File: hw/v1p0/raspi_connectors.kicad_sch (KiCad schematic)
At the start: 3 parts, among them J8 Raspberry_Pi_2_3

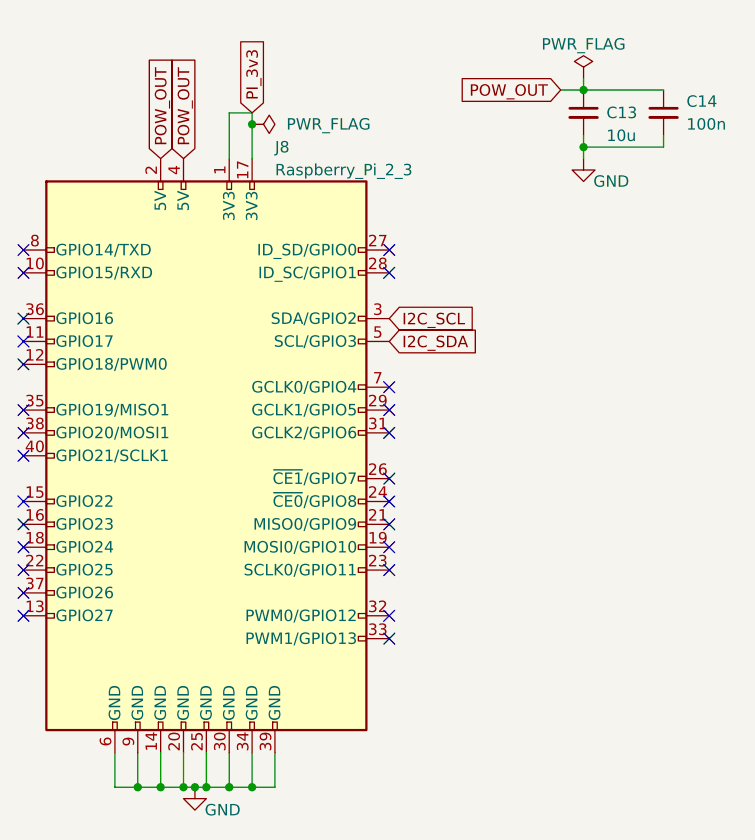
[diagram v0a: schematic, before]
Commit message: Last version before removing mosfet
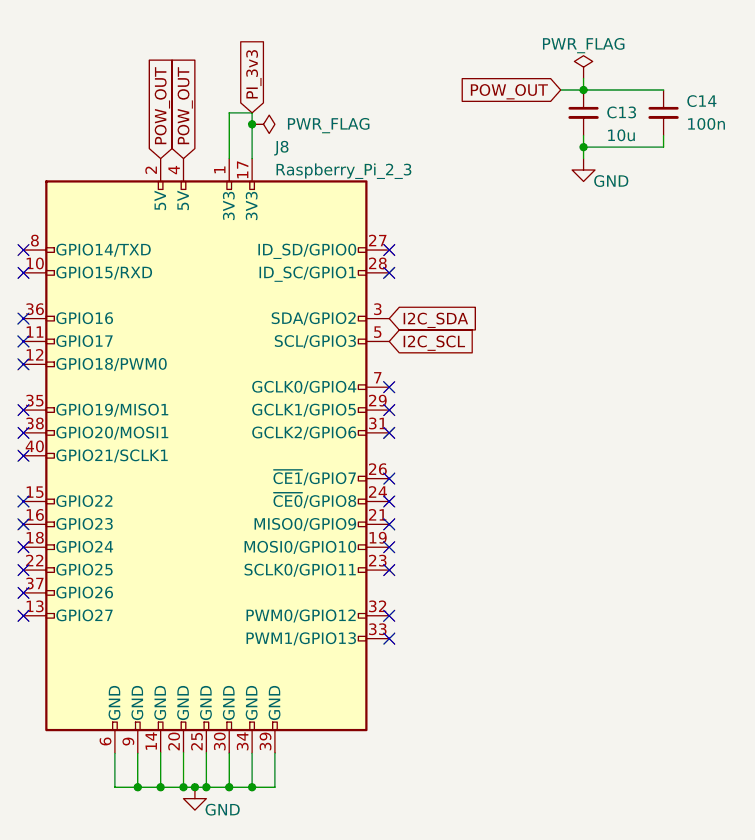
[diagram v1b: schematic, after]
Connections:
- net I2C_SCL: now also J8.5 (SCL/GPIO3); no longer J8.3 (SDA/GPIO2)
- net I2C_SDA: now also J8.3 (SDA/GPIO2); no longer J8.5 (SCL/GPIO3)
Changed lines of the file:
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@@
     )
   )
-  (global_label "I2C_SCL" (shape input) (at 81.28 49.53 0) (fields_autoplaced)
+  (global_label "I2C_SCL" (shape input) (at 81.28 52.07 0) (fields_autoplaced)
     (effects (font (size 1.27 1.27)) (justify left))
-    (property "Intersheet References" "${INTERSHEET_REFS}" (id 0) (at 91.2526 49.4506 0)
+    (property "Intersheet References" "${INTERSHEET_REFS}" (id 0) (at 91.2526 51.9906 0)
       (effects (font (size 1.27 1.27)) (justify left) hide)
     )
@@
     )
   )
-  (global_label "I2C_SDA" (shape input) (at 81.28 52.07 0) (fields_autoplaced)
+  (global_label "I2C_SDA" (shape input) (at 81.28 49.53 0) (fields_autoplaced)
     (effects (font (size 1.27 1.27)) (justify left))
-    (property "Intersheet References" "${INTERSHEET_REFS}" (id 0) (at 91.3131 51.9906 0)
+    (property "Intersheet References" "${INTERSHEET_REFS}" (id 0) (at 91.3131 49.4506 0)
       (effects (font (size 1.27 1.27)) (justify left) hide)
     )

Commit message: Removed Mosfet - release candidate 1.0
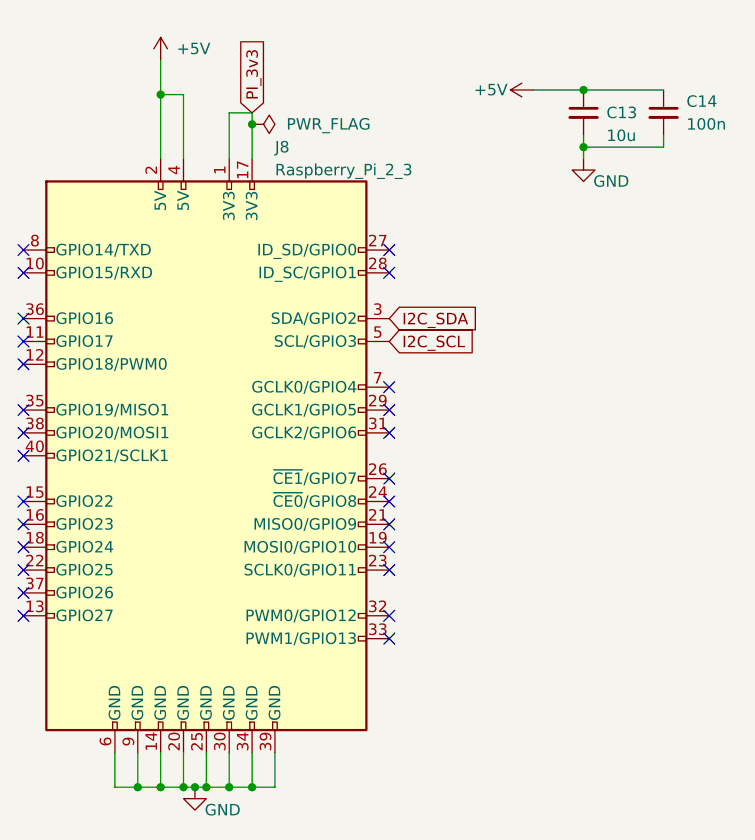
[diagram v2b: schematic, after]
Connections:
- net POW_OUT renamed +5V
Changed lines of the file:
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@@
   (junction (at 60.96 101.6) (diameter 0) (color 0 0 0 0)
+  )
+  (junction (at 55.88 24.638) (diameter 0) (color 0 0 0 0)
   )
   (no_connect (at 81.28 59.69))
@@
     (stroke (width 0) (type default) (color 0 0 0 0))
   )
+  (wire (pts (xy 55.88 24.638) (xy 55.88 31.75))
+    (stroke (width 0) (type default) (color 0 0 0 0))
+  )
   (wire (pts (xy 102.87 24.13) (xy 111.76 24.13))
     (stroke (width 0) (type default) (color 0 0 0 0))
@@
     (stroke (width 0) (type default) (color 0 0 0 0))
   )
-  (wire (pts (xy 102.87 22.86) (xy 102.87 24.13))
-    (stroke (width 0) (type default) (color 0 0 0 0))
-  )
   (wire (pts (xy 68.58 97.79) (xy 68.58 101.6))
     (stroke (width 0) (type default) (color 0 0 0 0))
@@
     (stroke (width 0) (type default) (color 0 0 0 0))
   )
-  (wire (pts (xy 100.33 24.13) (xy 102.87 24.13))
+  (wire (pts (xy 97.282 24.13) (xy 102.87 24.13))
     (stroke (width 0) (type default) (color 0 0 0 0))
   )
@@
     (stroke (width 0) (type default) (color 0 0 0 0))
   )
+  (wire (pts (xy 58.42 31.75) (xy 58.42 24.638))
+    (stroke (width 0) (type default) (color 0 0 0 0))
+  )
+  (wire (pts (xy 55.88 20.828) (xy 55.88 24.638))
+    (stroke (width 0) (type default) (color 0 0 0 0))
+  )
   (wire (pts (xy 102.87 29.21) (xy 102.87 30.48))
     (stroke (width 0) (type default) (color 0 0 0 0))
   )
+  (wire (pts (xy 58.42 24.638) (xy 55.88 24.638))
+    (stroke (width 0) (type default) (color 0 0 0 0))
+  )
   (wire (pts (xy 68.58 101.6) (xy 66.04 101.6))
     (stroke (width 0) (type default) (color 0 0 0 0))
@@
   (wire (pts (xy 58.42 101.6) (xy 59.69 101.6))
     (stroke (width 0) (type default) (color 0 0 0 0))
-  )
-  (global_label "POW_OUT" (shape input) (at 58.42 31.75 90) (fields_autoplaced)
-    (effects (font (size 1.27 1.27)) (justify left))
-    (property "Intersheet References" "${INTERSHEET_REFS}" (id 0) (at 58.3406 20.6888 90)
-      (effects (font (size 1.27 1.27)) (justify left) hide)
-    )
   )
   (global_label "I2C_SCL" (shape input) (at 81.28 52.07 0) (fields_autoplaced)
@@
     )
   )
-  (global_label "POW_OUT" (shape input) (at 55.88 31.75 90) (fields_autoplaced)
-    (effects (font (size 1.27 1.27)) (justify left))
-    (property "Intersheet References" "${INTERSHEET_REFS}" (id 0) (at 55.8006 20.6888 90)
-      (effects (font (size 1.27 1.27)) (justify left) hide)
-    )
-  )
   (global_label "I2C_SDA" (shape input) (at 81.28 49.53 0) (fields_autoplaced)
     (effects (font (size 1.27 1.27)) (justify left))
@@
     )
   )
-  (global_label "POW_OUT" (shape input) (at 100.33 24.13 180) (fields_autoplaced)
-    (effects (font (size 1.27 1.27)) (justify right))
-    (property "Intersheet References" "${INTERSHEET_REFS}" (id 0) (at 89.2688 24.2094 0)
-      (effects (font (size 1.27 1.27)) (justify right) hide)
-    )
-  )
   (global_label "PI_3v3" (shape input) (at 66.04 26.67 90) (fields_autoplaced)
     (effects (font (size 1.27 1.27)) (justify left))
@@
     (pin "1")
   )
-  (symbol (lib_id "power:PWR_FLAG") (at 102.87 22.86 0) (unit 1)
-    (in_bom yes) (on_board yes)
-    (property "Reference" "#FLG03" (id 0) (at 102.87 20.955 0)
-      (effects (font (size 1.27 1.27)) hide)
-    )
-    (property "Value" "PWR_FLAG" (id 1) (at 102.87 19.05 0))
-    (property "Footprint" "" (id 2) (at 102.87 22.86 0)
-      (effects (font (size 1.27 1.27)) hide)
-    )
-    (property "Datasheet" "~" (id 3) (at 102.87 22.86 0)
+  (symbol (lib_id "power:+5V") (at 55.88 20.828 0) (unit 1)
+    (in_bom yes) (on_board yes) (fields_autoplaced)
+    (property "Reference" "#PWR08" (id 0) (at 55.88 24.638 0)
+      (effects (font (size 1.27 1.27)) hide)
+    )
+    (property "Value" "+5V" (id 1) (at 57.658 19.5579 0)
+      (effects (font (size 1.27 1.27)) (justify left))
+    )
+    (property "Footprint" "" (id 2) (at 55.88 20.828 0)
+      (effects (font (size 1.27 1.27)) hide)
+    )
+    (property "Datasheet" "" (id 3) (at 55.88 20.828 0)
       (effects (font (size 1.27 1.27)) hide)
     )
@@
     (pin "2")
   )
+  (symbol (lib_id "power:+5V") (at 97.282 24.13 90) (unit 1)
+    (in_bom yes) (on_board yes)
+    (property "Reference" "#PWR022" (id 0) (at 101.092 24.13 0)
+      (effects (font (size 1.27 1.27)) hide)
+    )
+    (property "Value" "+5V" (id 1) (at 90.678 24.13 90)
+      (effects (font (size 1.27 1.27)) (justify right))
+    )
+    (property "Footprint" "" (id 2) (at 97.282 24.13 0)
+      (effects (font (size 1.27 1.27)) hide)
+    )
+    (property "Datasheet" "" (id 3) (at 97.282 24.13 0)
+      (effects (font (size 1.27 1.27)) hide)
+    )
+    (pin "1")
+  )
   (symbol (lib_id "Device:C_Small") (at 102.87 26.67 0) (unit 1)
